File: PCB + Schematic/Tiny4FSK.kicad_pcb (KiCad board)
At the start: 4 copper layers, 35.1 x 76.3 mm, 90 parts, among them J1 Power Ext, J2 GPIO, J3 I2C, J4 USB, J5 USB Breakout, J6 SPI, J7 USBC, J8 SWD, SW1 Power Switch, SW2 RST, U1 BME280, U2 ATGM336H, U3 TPS61200DRC, U4 ECS-327TXO-2012, U5 ATSAMD21G18A-A, U6 SI4063, U7 Linear Step-Down

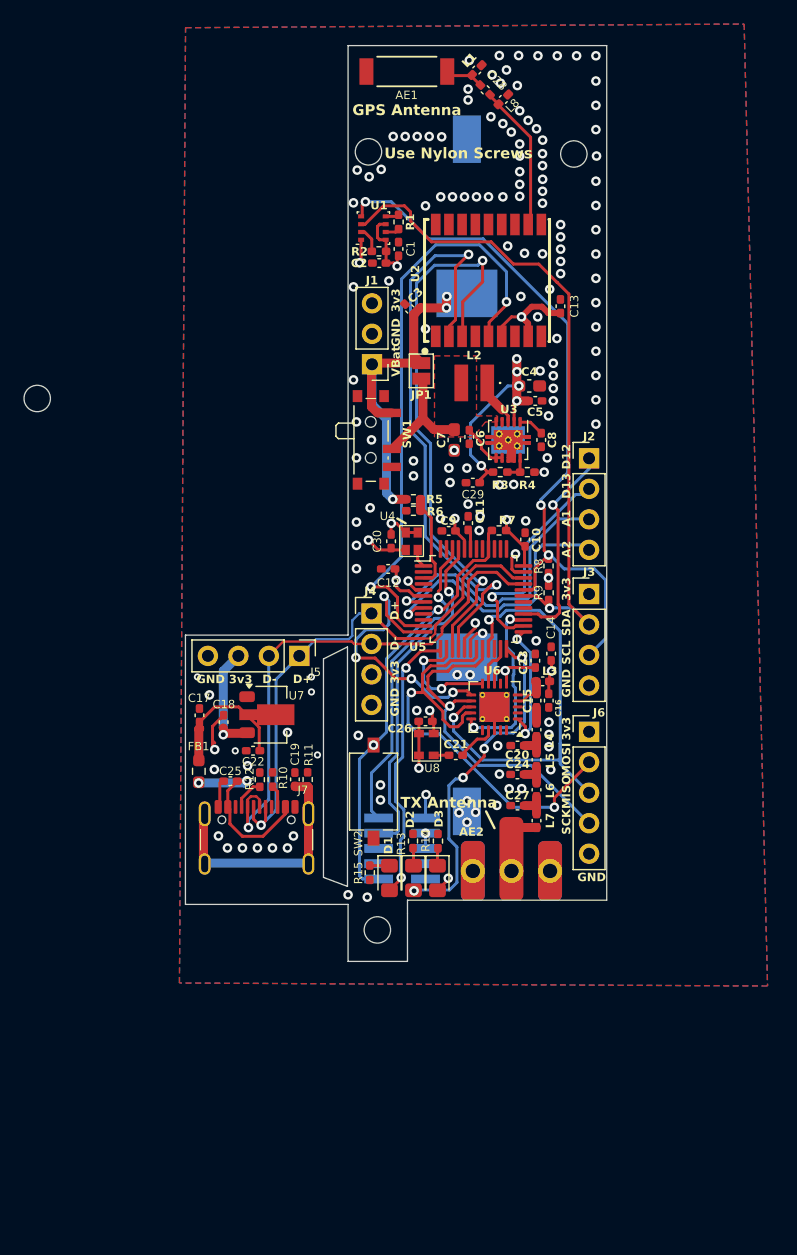
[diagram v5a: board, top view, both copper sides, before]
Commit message: small updates to PCB, revamp README
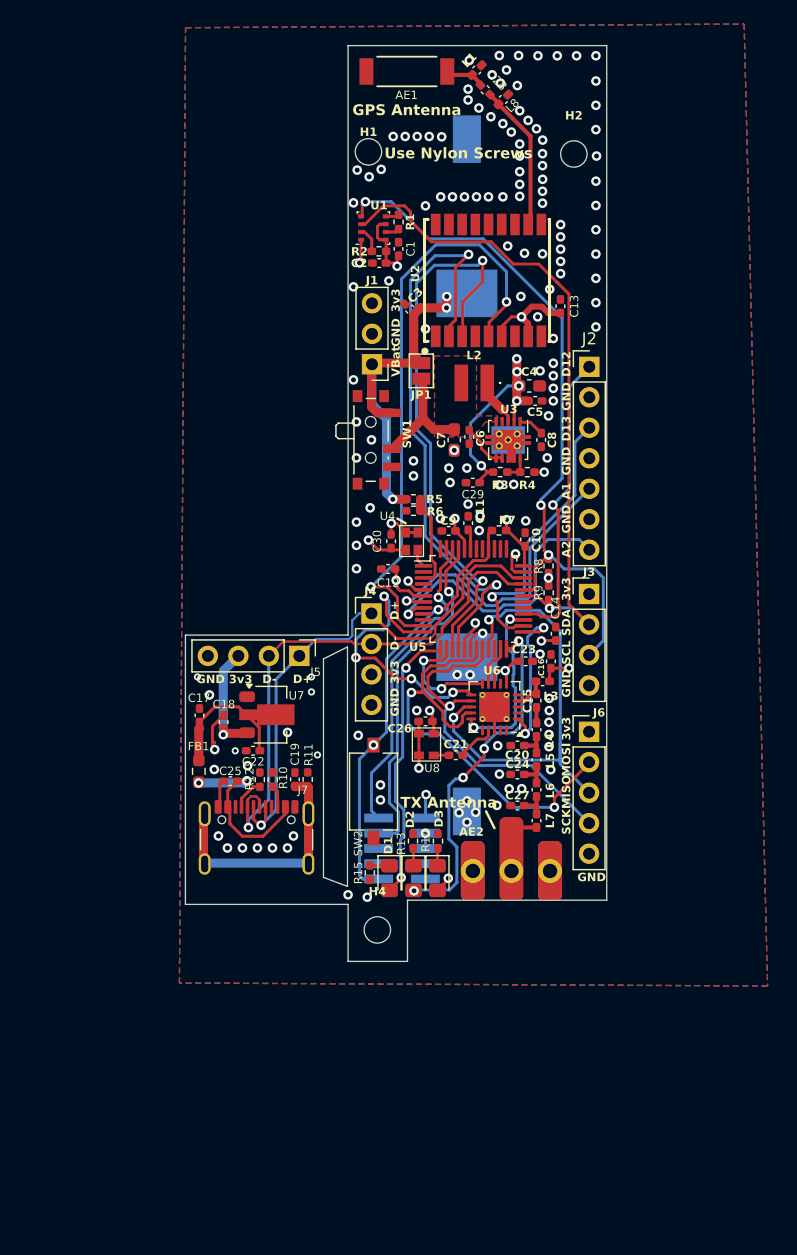
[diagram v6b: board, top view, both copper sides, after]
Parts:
- removed H3: MountingHole, MountingHole:MountingHole_2.2mm_M2
- J2: footprint Connector_PinHeader_2.54mm:PinHeader_1x04_P2.54mm_Vertical -> Connector_PinHeader_2.54mm:PinHeader_1x07_P2.54mm_Vertical
- moved J2 7.63 mm to (160.4, 63.7)
- moved C16 3.27 mm to (157.2, 88.2), turned to -90 degrees
- moved C14 1.70 mm to (157.6, 85.9)
- moved C23 0.80 mm to (155.1, 88.2), turned to 0 degrees
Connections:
- J2 pad 2: D13 -> Earth
- J2 pad 3: A1 -> D13
- J2 pad 4: A2 -> Earth
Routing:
- net D12: track 17.6 -> 25.2 mm
- net D13: track 18.6 -> 23.3 mm
- net Net-(AE2-RF): track 5.49 -> 9.49 mm
- net SDN: track 10.8 -> 13.3 mm
- net MOSI: track 37.4 -> 39.2 mm
- net A1: track 24.0 -> 25.7 mm
- net ERROR: track 28.3 -> 29.3 mm
- net A2: track 23.6 -> 24.6 mm
- net SCL: track 59.5 -> 59.0 mm
- net +3.3V: track 73.1 -> 72.9 mm, vias 19 -> 20
- net Earth: vias 151 -> 150
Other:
- board text added: "+"
- board text added: "-"

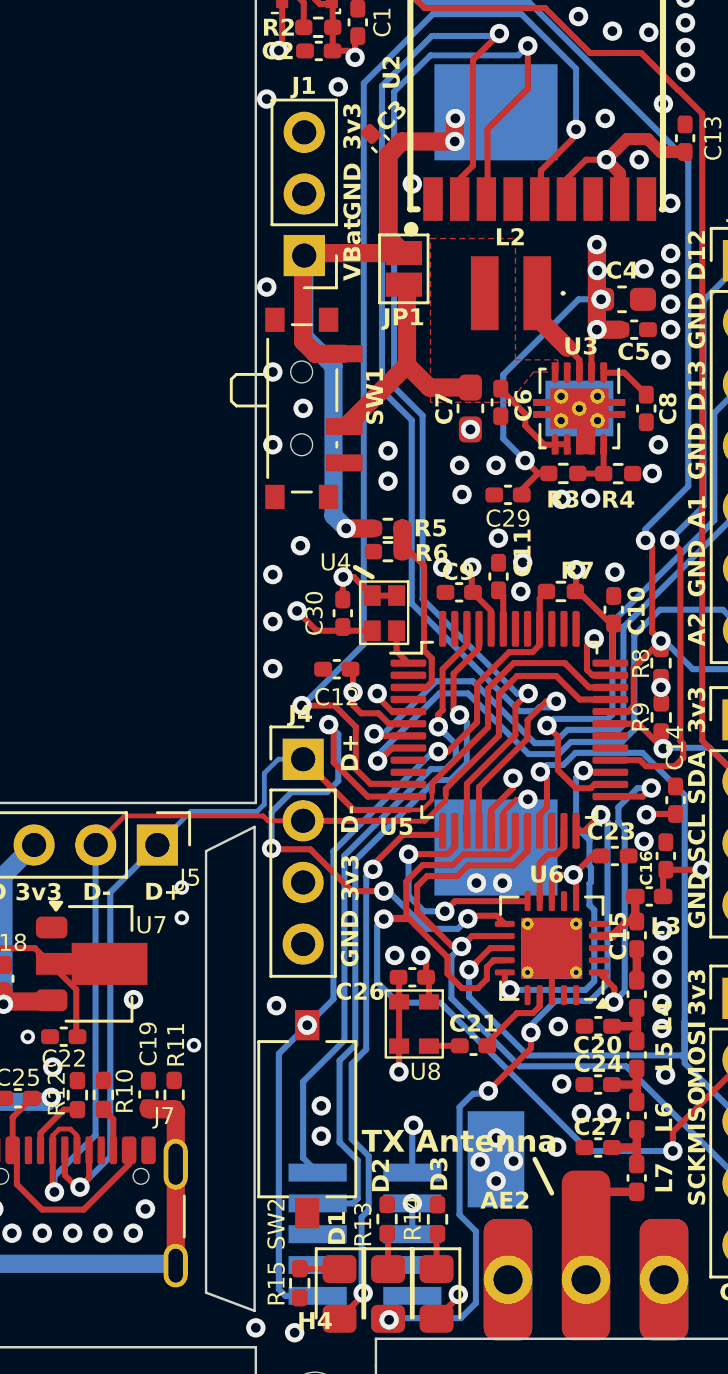
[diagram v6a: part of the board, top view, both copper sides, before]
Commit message: Make PCB more production-friendly
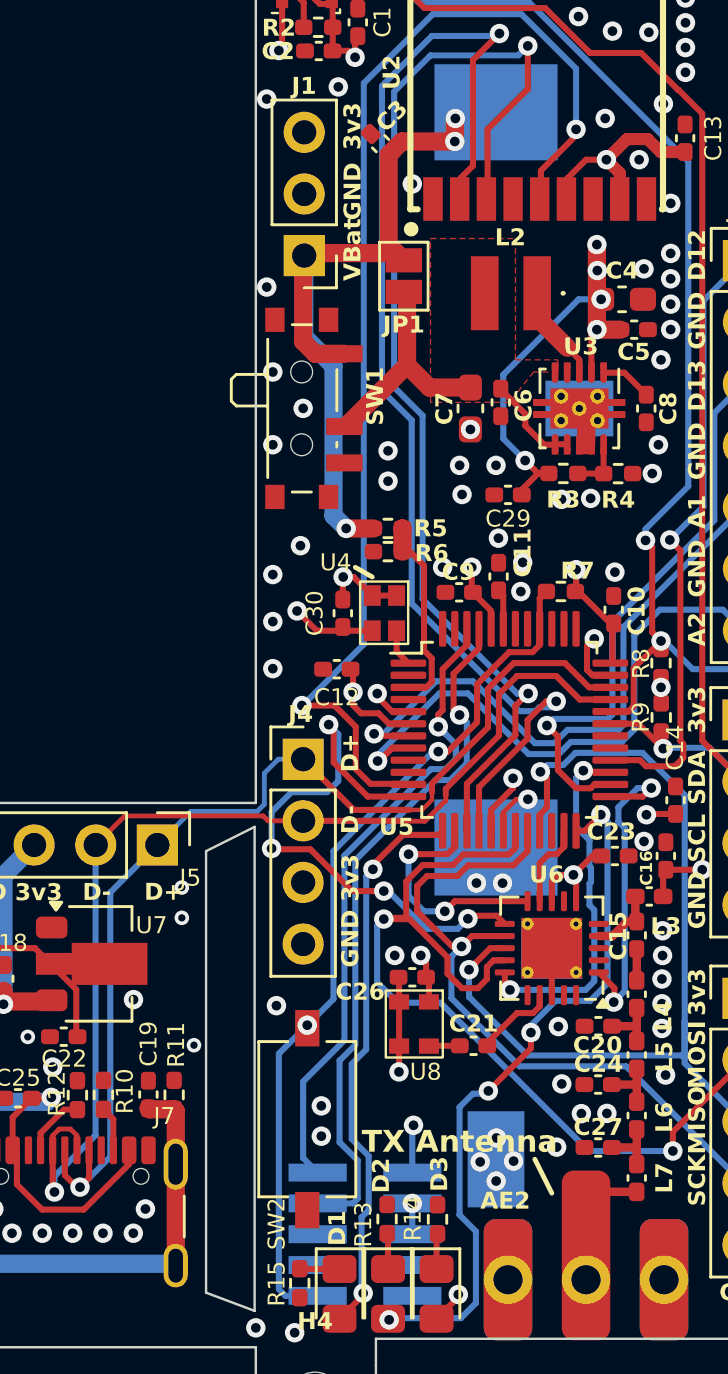
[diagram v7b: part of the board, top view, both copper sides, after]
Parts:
- moved JP1 0.30 mm to (146.4, 64.3)
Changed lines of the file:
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@@
 		(49 "F.Fab" user)
 		(50 "User.1" user)
-		(51 "User.2" user)
+		(51 "User.2" user "SMT-Orientation")
 		(52 "User.3" user)
 		(53 "User.4" user)
@@
 		(allow_soldermask_bridges_in_footprints no)
 		(pcbplotparams
-			(layerselection 0x00010fc_ffffffff)
+			(layerselection 0x00810fc_ffffffff)
 			(plot_on_all_layers_selection 0x0000000_00000000)
 			(disableapertmacros no)
@@
 	(footprint "Jumper:SolderJumper-2_P1.3mm_Open_Pad1.0x1.5mm"
 		(layer "F.Cu")
-		(at 146.4 64 90)
+		(at 146.4 64.3 90)
 		(descr "SMD Solder Jumper, 1x1.5mm Pads, 0.3mm gap, open")
 		(tags "solder jumper open")
@@
 		(tags "capacitor handsolder")
 		(property "Reference" "C23"
-			(at -0.15 -1 360)
+			(at -0.15 -1 0)
 			(layer "F.SilkS")
 			(effects
@@
 		)
 		(property "Value" "100nF"
-			(at 0 1.16 360)
+			(at 0 1.16 0)
 			(layer "F.Fab")
 			(effects
@@
 		)
 		(fp_text user "${REFERENCE}"
-			(at 0 0 360)
+			(at 0 0 0)
 			(layer "F.Fab")
 			(effects
@@
 		)
 		(pad "1" smd rect
-			(at -3.875 0 90)
-			(size 1.25 1)
+			(at -3.75 0 90)
+			(size 1.5 1)
 			(layers "F.Cu" "F.Paste" "F.Mask")
 			(net 1 "Earth")
@@
 		)
 		(pad "2" smd rect
-			(at 3.875 0 90)
-			(size 1.25 1)
+			(at 3.75 0 90)
+			(size 1.5 1)
 			(layers "F.Cu" "F.Paste" "F.Mask")
 			(net 20 "nRST")
@@
 	)
 	(segment
-		(start 146.4 64.65)
-		(end 146.5325 64.7825)
+		(start 146.4 64.95)
+		(end 146.5325 65.0825)
 		(width 0.75)
 		(layer "F.Cu")
@@
 	)
 	(segment
-		(start 146.5325 64.7825)
-		(end 146.5325 67.9675)
-		(width 0.75)
-		(layer "F.Cu")
-		(net 6)
-	)
-	(segment
 		(start 152.62 71.23)
 		(end 152.6 71.25)
@@
 	)
 	(segment
+		(start 146.5325 65.0825)
+		(end 146.5325 67.9675)
+		(width 0.75)
+		(layer "F.Cu")
+		(net 6)
+	)
+	(segment
 		(start 149.145 68.8925)
 		(end 147.4575 68.8925)
@@
 	)
 	(segment
-		(start 142.294431 63.452157)
-		(end 142.396588 63.35)
+		(start 146.3175 58.75)
+		(end 148.5 58.75)
 		(width 0.75)
 		(layer "F.Cu")
@@
 	)
 	(segment
-		(start 142.396588 63.35)
-		(end 146.4 63.35)
+		(start 145.775 59.2925)
+		(end 146.3175 58.75)
+		(width 0.75)
+		(layer "F.Cu")
+		(net 40)
+	)
+	(segment
+		(start 146.1 63.35)
+		(end 146.4 63.65)
 		(width 0.75)
 		(layer "F.Cu")
@@
 	)
 	(segment
-		(start 146.3175 58.75)
-		(end 148.5 58.75)
+		(start 145.775 63.025)
+		(end 145.775 59.2925)
 		(width 0.75)
 		(layer "F.Cu")
@@
 	)
 	(segment
-		(start 148.5 57.824906)
-		(end 148.525 57.799906)
+		(start 146.4 63.65)
+		(end 145.775 63.025)
 		(width 0.75)
 		(layer "F.Cu")
@@
 	)
 	(segment
-		(start 142.25 63.496588)
-		(end 142.25 67)
+		(start 148.5 57.824906)
+		(end 148.525 57.799906)
 		(width 0.75)
 		(layer "F.Cu")
@@
 	)
 	(segment
-		(start 145.775 62.725)
-		(end 145.775 59.2925)
+		(start 142.25 63.496588)
+		(end 142.25 67)
 		(width 0.75)
 		(layer "F.Cu")
@@
 	)
 	(segment
-		(start 146.4 63.35)
-		(end 145.775 62.725)
+		(start 142.396588 63.35)
+		(end 146.1 63.35)
 		(width 0.75)
 		(layer "F.Cu")
@@
 	)
 	(segment
-		(start 148.5 58.75)
-		(end 148.5 57.824906)
+		(start 142.294431 63.452157)
+		(end 142.396588 63.35)
 		(width 0.75)
 		(layer "F.Cu")
@@
 	)
 	(segment
-		(start 145.775 59.2925)
-		(end 146.3175 58.75)
+		(start 148.5 58.75)
+		(end 148.5 57.824906)
 		(width 0.75)
 		(layer "F.Cu")

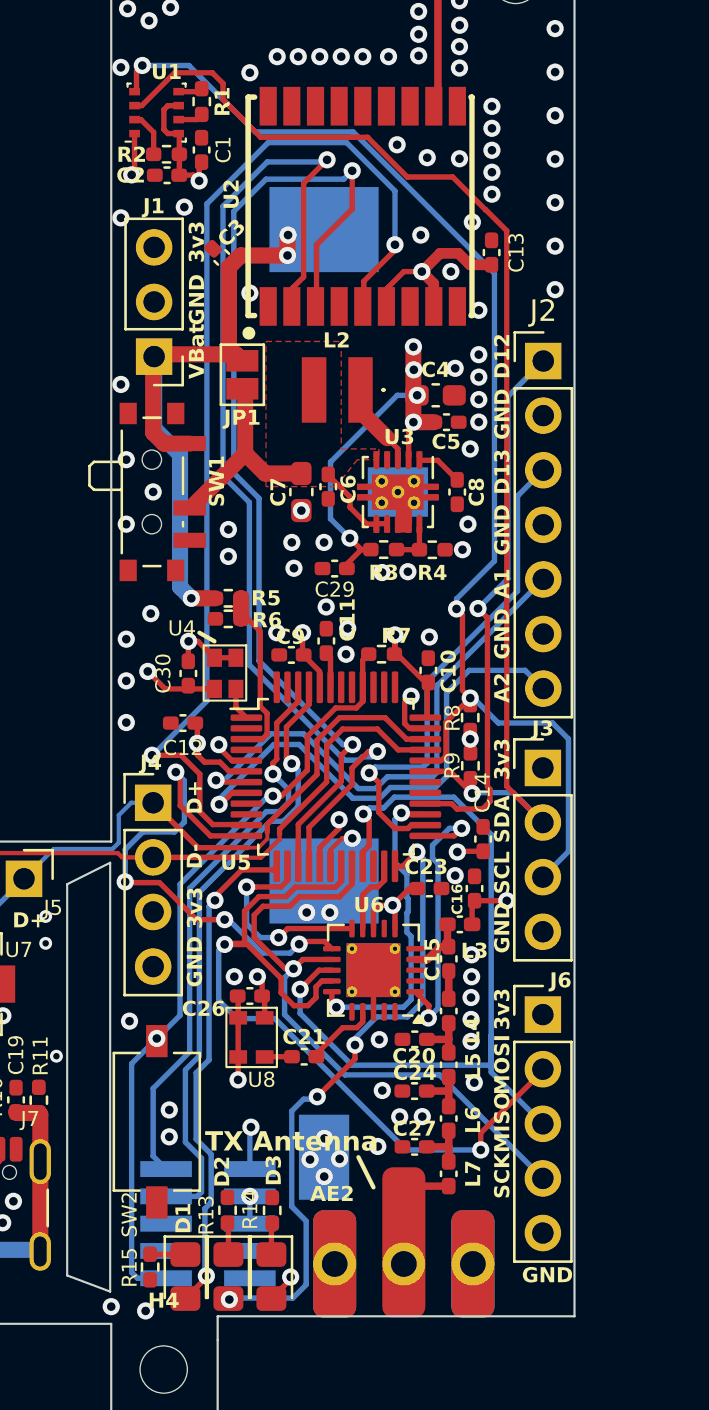
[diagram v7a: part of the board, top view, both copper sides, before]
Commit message: Refactor Tiny4FSK project files and add shield functionality
- Updated Tiny4FSK.kicad_pro to include layer_pairs and changed the 3D model reference to Tiny4FSK-simple.step.
- Modified Tiny4FSK.kicad_sch to replace a 7-pin connector with a 9-pin connector, adjusting pin positions and properties accordingly.
- Introduced new shield.cpp and shield.h files to support interaction with the Tiny4FSK General Shield, including I2C scanning and initialization for BME280, IMU, and OLED devices.
- Added a new 3D model file Tiny4FSK-simple.step.
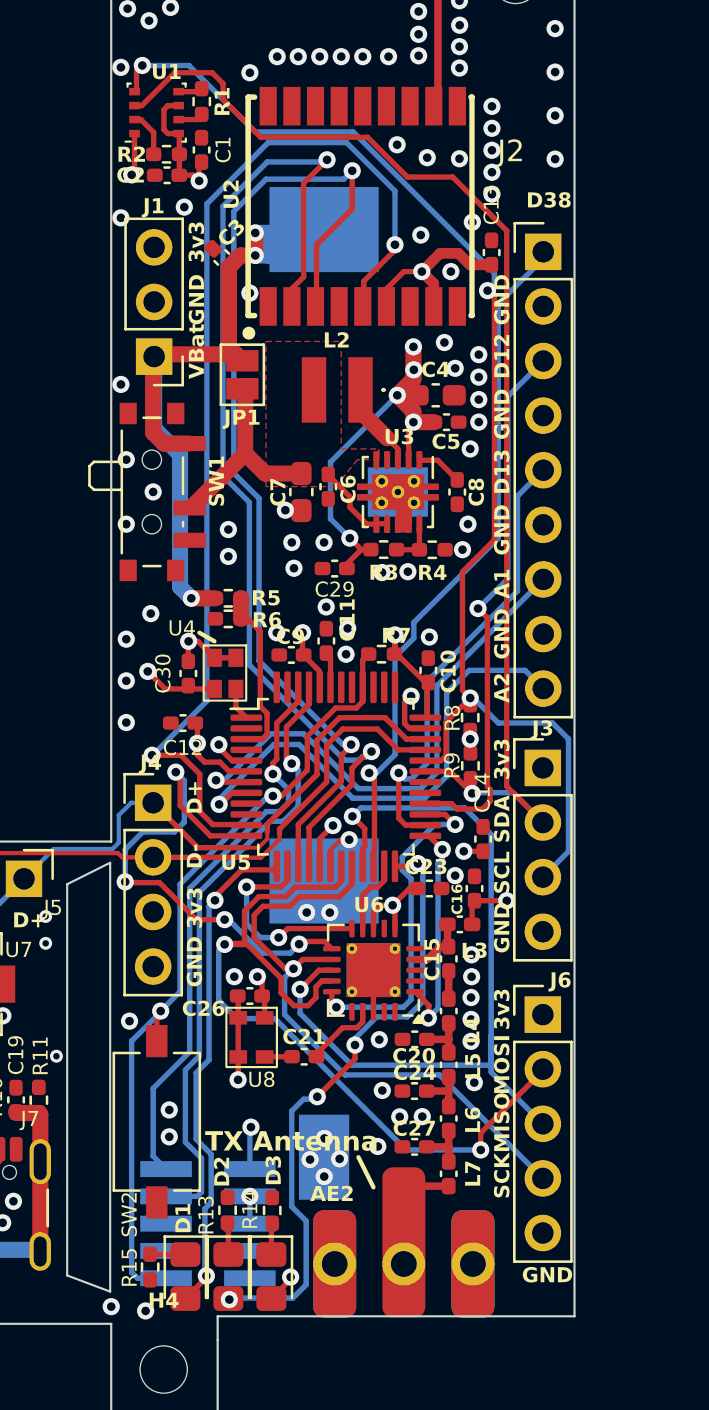
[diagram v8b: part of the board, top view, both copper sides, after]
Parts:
- J2: footprint Connector_PinHeader_2.54mm:PinHeader_1x07_P2.54mm_Vertical -> Connector_PinHeader_2.54mm:PinHeader_1x09_P2.54mm_Vertical
- moved J2 5.08 mm to (160.4, 58.6)
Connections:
- J2 pad 1: D12 -> D38
- J2 pad 3: D13 -> D12
- J2 pad 5: A1 -> D13
- J2 pad 7: A2 -> A1
- U5 pad 22: unconnected-(U5-PA13-Pad22) -> D38
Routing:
- net D38: track 0.00 -> 32.3 mm, vias 0 -> 1
- net +BATT: track 32.0 -> 40.8 mm
- net SDN: track 13.3 -> 10.7 mm
- net D13: track 23.3 -> 21.1 mm
- net nRST: track 36.0 -> 37.4 mm
- net RF_SS: track 14.7 -> 15.9 mm
- net +3.3V: track 72.9 -> 71.8 mm
- net ERROR: track 29.3 -> 28.6 mm
- net RXD: track 49.9 -> 49.4 mm
- net Earth: track 28.9 -> 28.8 mm, vias 150 -> 147
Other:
- board text added: "D38"
